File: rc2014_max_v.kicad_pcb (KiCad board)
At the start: 2 copper layers, 101.6 x 50.8 mm, 12 parts, among them IC1 SN74ALVC164245DGG, IC2 5M570ZT100I5N, IC3 SN74ALVC164245DGG, J1 Z80 Bus, J2 Pro Bus, J4 M3 Mounting Hole, U1 MIC5356-SGYMME, U2 SN74AVC8T245PW

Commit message: reorganized pins
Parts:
- removed IC1, IC3: SN74ALVC164245DGG, Package_SO:TSSOP-48_6.1x12.5mm_P0.5mm
- removed IC2: 5M570ZT100I5N, QFP50P1600X1600X120-100N:QFP50P1600X1600X120-100N
- added C10: 100nF, Capacitor_SMD:C_0805_2012Metric_Pad1.15x1.40mm_HandSolder, F.Cu at (101.9, 91.8)
- added C11: 100nF, Capacitor_SMD:C_0805_2012Metric_Pad1.15x1.40mm_HandSolder, F.Cu at (96.0, 103.5)
- added C12: 100nF, Capacitor_SMD:C_0805_2012Metric_Pad1.15x1.40mm_HandSolder, F.Cu at (101.6, 95.9)
- added C13: 100nF, Capacitor_SMD:C_0805_2012Metric_Pad1.15x1.40mm_HandSolder, F.Cu at (106.7, 91.8)
- added C14: 100nF, Capacitor_SMD:C_0805_2012Metric_Pad1.15x1.40mm_HandSolder, F.Cu at (101.5, 103.5)
- added C15: 100nF, Capacitor_SMD:C_0805_2012Metric_Pad1.15x1.40mm_HandSolder, F.Cu at (106.4, 95.9)
- added C16: 100nF, Capacitor_SMD:C_0805_2012Metric_Pad1.15x1.40mm_HandSolder, F.Cu at (106.4, 98.9)
- added C5: 100nF, Capacitor_SMD:C_0805_2012Metric_Pad1.15x1.40mm_HandSolder, F.Cu at (92.4, 91.8)
- added C6: 100nF, Capacitor_SMD:C_0805_2012Metric_Pad1.15x1.40mm_HandSolder, F.Cu at (101.6, 115.4)
- added C7: 100nF, Capacitor_SMD:C_0805_2012Metric_Pad1.15x1.40mm_HandSolder, F.Cu at (97.2, 91.8)
- added C8: 100nF, Capacitor_SMD:C_0805_2012Metric_Pad1.15x1.40mm_HandSolder, F.Cu at (96.1, 115.4)
- added C9: 100nF, Capacitor_SMD:C_0805_2012Metric_Pad1.15x1.40mm_HandSolder, F.Cu at (96.9, 95.9)
- added U3: SN74ALVC164245DGG, Package_SO:TSSOP-48_6.1x12.5mm_P0.5mm, F.Cu at (97.7, 109.4)
- added U4: 5M570ZT100I5N, Package_QFP:TQFP-100_14x14mm_P0.5mm, F.Cu at (130.0, 88.9)
- added U5: SN74ALVC164245DGG, Package_SO:TSSOP-48_6.1x12.5mm_P0.5mm, F.Cu at (154.9, 109.0)
- C1, C2, C3, C4: footprint Capacitor_THT:C_Disc_D3.8mm_W2.6mm_P2.50mm -> Capacitor_SMD:C_0805_2012Metric_Pad1.15x1.40mm_HandSolder; moved to B.Cu
- U1: moved to B.Cu
- U2: value SN74AVC8T245PW -> SN74ALVC164245DGG; footprint Package_SO:TSSOP-24_4.4x7.8mm_P0.65mm -> Package_SO:TSSOP-48_6.1x12.5mm_P0.5mm
- moved C2 35.3 mm to (125.8, 117.9)
- moved C4 35.3 mm to (131.4, 117.9)
- moved U1 35.3 mm to (127.8, 113.6)
- moved C3 35.3 mm to (133.0, 113.4)
- moved U2 6.77 mm to (132.5, 109.0)
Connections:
- J1 pad 20: (no net) -> ~RESET
- J1 pad 22: (no net) -> ~INT
- J2 pad 10: (no net) -> ~NMI
- J2 pad 4: (no net) -> ~RESET2
- J2 pad 7: (no net) -> ~HALT
- J2 pad 8: (no net) -> ~BUSRQ
- J2 pad 9: (no net) -> ~WAIT
- U2 pad 1: (no net) -> DIR
- U2 pad 10: (no net) -> GND
- U2 pad 11: Net-(U2-Pad11) -> ~PAGE
- U2 pad 12: Net-(U2-Pad11) -> ~BUSACK
- U2 pad 13: Net-(U2-Pad11) -> ~RESET
- U2 pad 14: (no net) -> ~INT
- U2 pad 15: (no net) -> GND
- U2 pad 16: (no net) -> ~RESET2
- U2 pad 17: (no net) -> ~HALT
- U2 pad 18: (no net) -> 5V
- U2 pad 19: (no net) -> ~BUSRQ
- U2 pad 2: (no net) -> ~M1
- U2 pad 20: (no net) -> ~WAIT
- U2 pad 21: (no net) -> GND
- U2 pad 22: (no net) -> ~NMI
- U2 pad 24: (no net) -> ~DIR
- U2 pad 3: (no net) -> CLK
- U2 pad 4: (no net) -> GND
- U2 pad 5: (no net) -> ~MREQ
- U2 pad 6: (no net) -> ~WR
- U2 pad 7: (no net) -> 5V
- U2 pad 8: (no net) -> ~RD
- U2 pad 9: (no net) -> ~IORQ

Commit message: numerous changes
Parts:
- removed C13, C15: 100nF, Capacitor_SMD:C_0805_2012Metric_Pad1.15x1.40mm_HandSolder
- added C17: 100nF, Capacitor_SMD:C_0603_1608Metric_Pad1.05x0.95mm_HandSolder, F.Cu at (102.1, 83.3)
- added C18: 100nF, Capacitor_SMD:C_0603_1608Metric_Pad1.05x0.95mm_HandSolder, B.Cu at (95.2, 115.6)
- added C19: 100nF, Capacitor_SMD:C_0603_1608Metric_Pad1.05x0.95mm_HandSolder, B.Cu at (100.8, 115.6)
- added C20: 100nF, Capacitor_SMD:C_0603_1608Metric_Pad1.05x0.95mm_HandSolder, F.Cu at (128.0, 114.3)
- added C21: 100nF, Capacitor_SMD:C_0603_1608Metric_Pad1.05x0.95mm_HandSolder, F.Cu at (132.6, 114.3)
- added C22: 100nF, Capacitor_SMD:C_0603_1608Metric_Pad1.05x0.95mm_HandSolder, F.Cu at (157.2, 114.8)
- added C23: 100nF, Capacitor_SMD:C_0603_1608Metric_Pad1.05x0.95mm_HandSolder, F.Cu at (163.1, 114.8)
- added C24: 100nF, Capacitor_SMD:C_0603_1608Metric_Pad1.05x0.95mm_HandSolder, F.Cu at (126.2, 79.2)
- added C25: 100nF, Capacitor_SMD:C_0603_1608Metric_Pad1.05x0.95mm_HandSolder, F.Cu at (133.9, 79.2)
- added C26: 100nF, Capacitor_SMD:C_0603_1608Metric_Pad1.05x0.95mm_HandSolder, F.Cu at (133.7, 98.6)
- added C27: 100nF, Capacitor_SMD:C_0603_1608Metric_Pad1.05x0.95mm_HandSolder, F.Cu at (139.7, 90.7)
- added C28: 100nF, Capacitor_SMD:C_0603_1608Metric_Pad1.05x0.95mm_HandSolder, F.Cu at (119.4, 86.9)
- added C29: 100nF, Capacitor_SMD:C_0603_1608Metric_Pad1.05x0.95mm_HandSolder, F.Cu at (126.5, 98.6)
- added J3: Conn_01x06, Connector_PinHeader_2.54mm:PinHeader_1x06_P2.54mm_Horizontal, F.Cu at (173.0, 81.3)
- added J5: AVR-JTAG-10, Connector_IDC:IDC-Header_2x05_P2.54mm_Vertical, F.Cu at (159.5, 80.8)
- added J6: Conn_01x06, Connector_PinHeader_2.54mm:PinHeader_1x06_P2.54mm_Horizontal, F.Cu at (173.0, 98.0)
- added R1: 22R5, Resistor_SMD:R_0603_1608Metric_Pad1.05x0.95mm_HandSolder, F.Cu at (115.3, 85.9)
- added R2: 1K, Resistor_SMD:R_0603_1608Metric_Pad1.05x0.95mm_HandSolder, F.Cu at (110.0, 95.5)
- added R3: 1K, Resistor_SMD:R_0603_1608Metric_Pad1.05x0.95mm_HandSolder, F.Cu at (105.4, 95.5)
- added R4: 1K, Resistor_SMD:R_0603_1608Metric_Pad1.05x0.95mm_HandSolder, F.Cu at (107.7, 95.5)
- added SW1: SW_DIP_x03, Button_Switch_SMD:SW_DIP_SPSTx03_Slide_6.7x9.18mm_W8.61mm_P2.54mm_LowProfile, F.Cu at (96.8, 93.7)
- added U6: SN74ALVC164245DGG, Package_SO:TSSOP-48_6.1x12.5mm_P0.5mm, F.Cu at (160.0, 108.7)
- added X1: CB3LV-3I-50M0000, Oscillator:Oscillator_SMD_SeikoEpson_SG8002CA-4Pin_7.0x5.0mm_HandSoldering, F.Cu at (107.7, 83.3)
- C1, C10, C11, C12, C14, C16, C2, C3, C4, C7, C8, C9: footprint Capacitor_SMD:C_0805_2012Metric_Pad1.15x1.40mm_HandSolder -> Capacitor_SMD:C_0603_1608Metric_Pad1.05x0.95mm_HandSolder
- C5, C6: footprint Capacitor_SMD:C_0805_2012Metric_Pad1.15x1.40mm_HandSolder -> Capacitor_SMD:C_0603_1608Metric_Pad1.05x0.95mm_HandSolder; moved to B.Cu
- U2: value SN74ALVC164245DGG -> LTC6930IMS8 7.3728MHz; footprint Package_SO:TSSOP-48_6.1x12.5mm_P0.5mm -> Package_SO:MSOP-8_3x3mm_P0.65mm
- moved C10 62.1 mm to (163.1, 102.6)
- moved C9 60.2 mm to (156.7, 102.6)
- moved U5 57.7 mm to (97.3, 108.7)
- moved C12 39.2 mm to (139.7, 86.9), turned to 90 degrees
- moved C8 38.5 mm to (132.6, 103.1)
- moved U3 32.1 mm to (129.8, 108.7)
- moved C7 31.9 mm to (127.0, 103.1)
- moved C16 30.8 mm to (130.0, 79.2), turned to 180 degrees
- moved U2 30.4 mm to (107.7, 91.4), turned to 0 degrees
- moved C14 28.9 mm to (130.0, 98.6), turned to 180 degrees
- moved C11 26.6 mm to (119.4, 90.7), turned to 270 degrees
- moved C6 13.3 mm to (100.8, 102.1)
- moved C2 12.6 mm to (113.5, 114.8), turned to 180 degrees
- moved C5 10.7 mm to (95.2, 102.1)
- moved U1 9.49 mm to (118.6, 115.8)
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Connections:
- C10 pad 1: 5V -> +3V3
- C11 pad 1: +3V3 -> +1V8
- C12 pad 1: +3V3 -> +1V8
- C14 pad 1: +3V3 -> +1V8
- C16 pad 1: +3V3 -> +1V8
- C2 pad 2: Net-(C2-Pad2) -> GND
- C3 pad 2: Net-(C2-Pad2) -> GND
- C4 pad 2: Net-(C2-Pad2) -> GND
- C5 pad 1: 5V -> +3V3
- C6 pad 1: 5V -> +3V3
- C7 pad 1: 5V -> +3V3
- C8 pad 1: 5V -> +3V3
- C9 pad 1: 5V -> +3V3
- U1 pad 2: Net-(C2-Pad2) -> GND
- U1 pad 3: (no net) -> 5V
- U1 pad 9: Net-(C2-Pad2) -> GND
- U2 pad 1: DIR -> +3V3
- U2 pad 2: ~M1 -> GND
- U2 pad 3: CLK -> Net-(R4-Pad1)
- U2 pad 4: GND -> Net-(R3-Pad1)
- U2 pad 5: ~MREQ -> Net-(R2-Pad1)
- U2 pad 6: ~WR -> GND
- U2 pad 7: 5V -> (no net)
- U2 pad 8: ~RD -> +3V3
- U3 pad 11: A9 -> ~PAGE
- U3 pad 12: A8 -> ~BUSACK
- U3 pad 13: A7 -> ~RESET
- U3 pad 14: A6 -> ~INT
- U3 pad 16: A5 -> ~RESET2
- U3 pad 17: A4 -> ~HALT
- U3 pad 19: A3 -> ~BUSRQ
- U3 pad 2: A15 -> ~M1
- U3 pad 20: A2 -> ~WAIT
- U3 pad 22: A1 -> ~NMI
- U3 pad 23: A0 -> (no net)
- U3 pad 24: DIR -> ~DIR
- U3 pad 3: A14 -> CLK
- U3 pad 5: A13 -> ~MREQ
- U3 pad 6: A12 -> ~WR
- U3 pad 8: A11 -> ~RD
- U3 pad 9: A10 -> ~IORQ
- U4 pad 13: +3V3 -> +1V8
- U4 pad 31: +1V8 -> +3V3
- U4 pad 39: +3V3 -> +1V8
- U4 pad 45: +1V8 -> +3V3
- U4 pad 59: +1V8 -> +3V3
- U4 pad 63: +3V3 -> +1V8
- U4 pad 80: +1V8 -> +3V3
- U4 pad 88: +3V3 -> +1V8
- U4 pad 9: +1V8 -> +3V3
- U4 pad 94: +1V8 -> +3V3
- U5 pad 11: ~PAGE -> A9
- U5 pad 12: ~BUSACK -> A8
- U5 pad 13: D0 -> A7
- U5 pad 14: D1 -> A6
- U5 pad 16: D2 -> A5
- U5 pad 17: D3 -> A4
- U5 pad 19: D4 -> A3
- U5 pad 2: ~M1 -> A15
- U5 pad 20: D5 -> A2
- U5 pad 22: D6 -> A1
- U5 pad 23: D7 -> A0
- U5 pad 24: ~DIR -> DIR
- U5 pad 3: CLK -> A14
- U5 pad 5: ~MREQ -> A13
- U5 pad 6: ~WR -> A12
- U5 pad 8: ~RD -> A11
- U5 pad 9: ~IORQ -> A10
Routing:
- net +3V3: track 0.00 -> 56.8 mm, vias 0 -> 3
- net GND: track 6.54 -> 62.1 mm, vias 0 -> 4
- net 5V: track 6.16 -> 40.2 mm, vias 0 -> 2
- net Net-(R2-Pad1): track 0.00 -> 26.3 mm
- net A15: track 0.00 -> 20.5 mm
- net A0: track 0.72 -> 20.8 mm
- net Net-(R3-Pad1): track 0.00 -> 18.4 mm
- net A14: track 0.00 -> 18.3 mm
- net A1: track 0.00 -> 18.1 mm
- net A13: track 0.00 -> 17.7 mm
- net A2: track 0.00 -> 17.4 mm
- net A12: track 0.00 -> 16.8 mm
- net A3: track 0.36 -> 17.0 mm
- net A11: track 0.00 -> 16.3 mm
- net A4: track 0.73 -> 16.8 mm
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
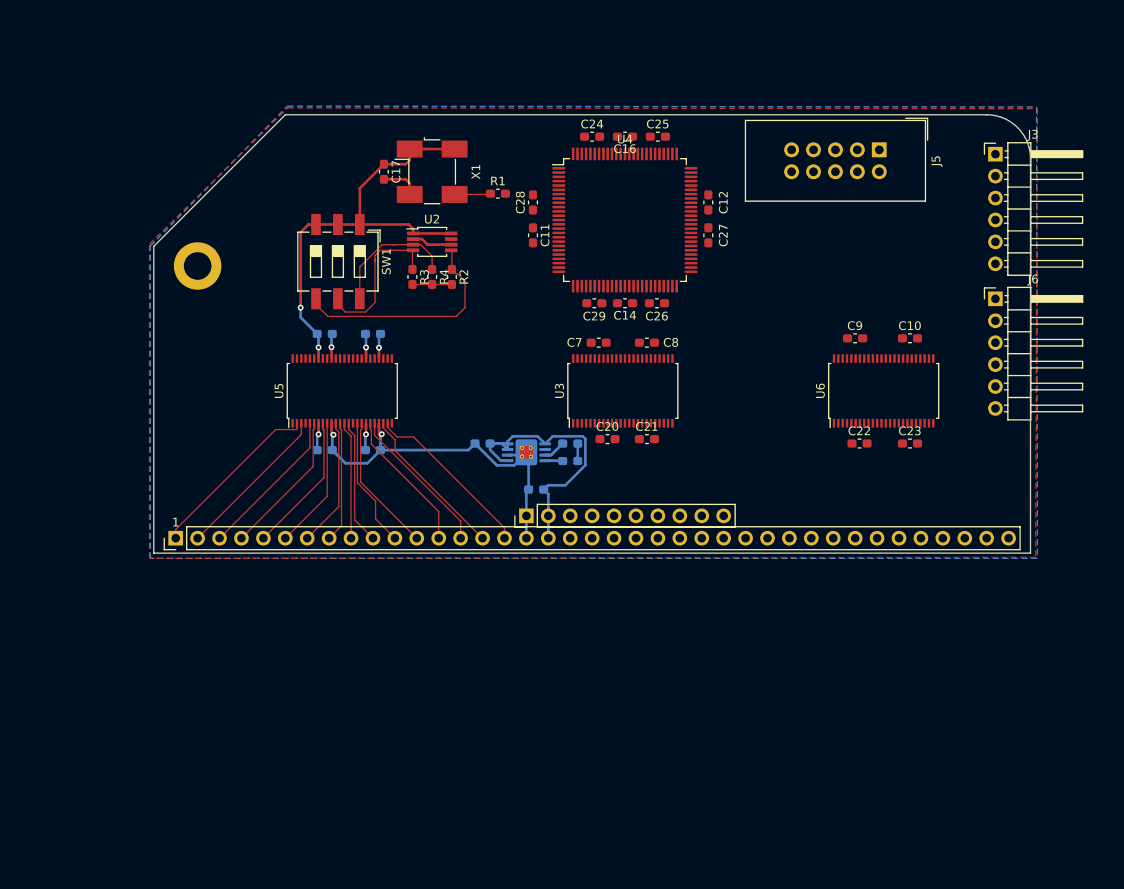
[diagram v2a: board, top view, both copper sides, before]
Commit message: added FT JTAG
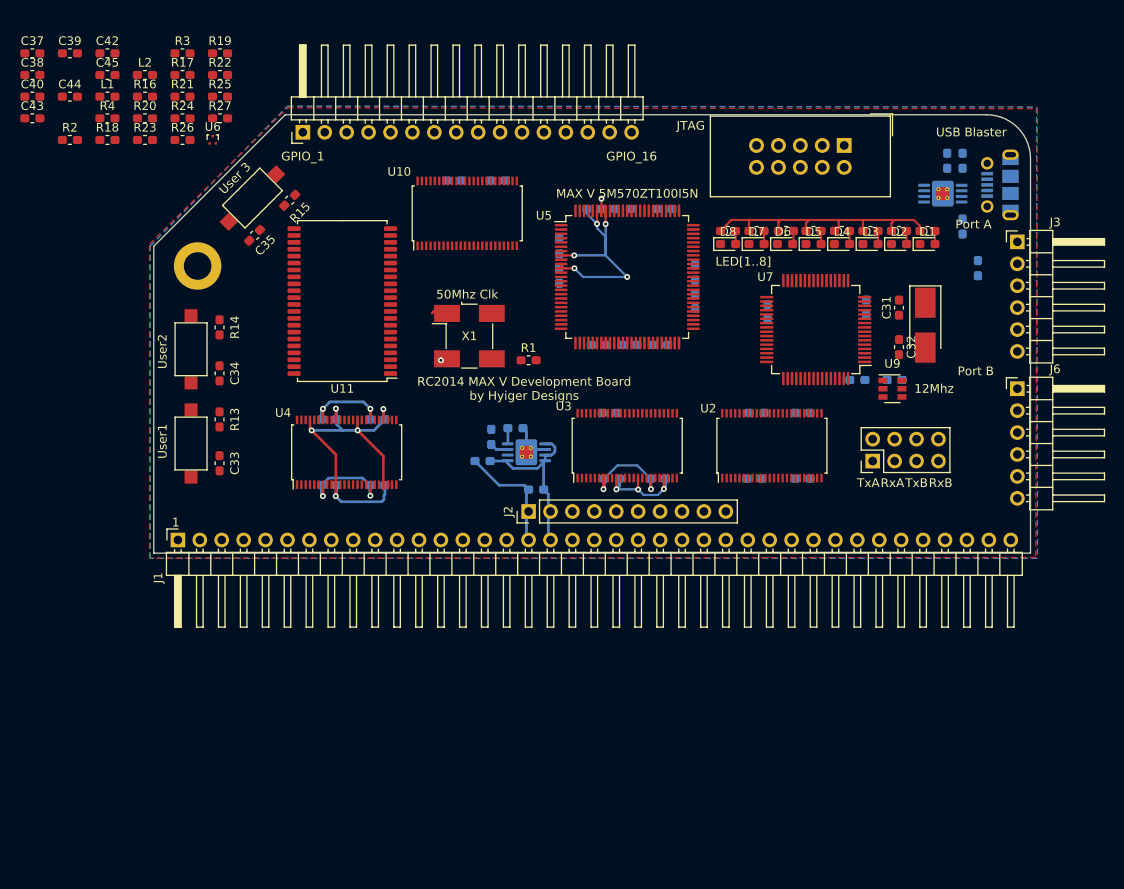
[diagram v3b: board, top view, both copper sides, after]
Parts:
- removed SW1: SW_DIP_x03, Button_Switch_SMD:SW_DIP_SPSTx03_Slide_6.7x9.18mm_W8.61mm_P2.54mm_LowProfile
- added C13: 100nF, Capacitor_SMD:C_0603_1608Metric_Pad1.05x0.95mm_HandSolder, B.Cu at (145.3, 111.3)
- added C15: 100nF, Capacitor_SMD:C_0603_1608Metric_Pad1.05x0.95mm_HandSolder, B.Cu at (128.3, 111.3)
- added C30: 100nF, Capacitor_SMD:C_0603_1608Metric_Pad1.05x0.95mm_HandSolder, B.Cu at (167.4, 82.0)
- added C31: 18pF, Capacitor_SMD:C_0603_1608Metric_Pad1.05x0.95mm_HandSolder, F.Cu at (161.8, 99.1)
- added C32: 18pF, Capacitor_SMD:C_0603_1608Metric_Pad1.05x0.95mm_HandSolder, F.Cu at (161.8, 103.6)
- added C33: 100nF, Capacitor_SMD:C_0603_1608Metric_Pad1.05x0.95mm_HandSolder, F.Cu at (83.1, 117.1)
- added C34: 100nF, Capacitor_SMD:C_0603_1608Metric_Pad1.05x0.95mm_HandSolder, F.Cu at (83.1, 106.7)
- added C35: 100nF, Capacitor_SMD:C_0603_1608Metric_Pad1.05x0.95mm_HandSolder, F.Cu at (87.1, 90.7)
- added C36: 100nF, Capacitor_SMD:C_0603_1608Metric_Pad1.05x0.95mm_HandSolder, B.Cu at (110.2, 84.3)
- added C37: 4.7uF, Capacitor_SMD:C_0603_1608Metric_Pad1.05x0.95mm_HandSolder, F.Cu at (61.4, 69.6)
- added C38: 100nF, Capacitor_SMD:C_0603_1608Metric_Pad1.05x0.95mm_HandSolder, F.Cu at (61.4, 72.1)
- added C39: 4.7uF, Capacitor_SMD:C_0603_1608Metric_Pad1.05x0.95mm_HandSolder, F.Cu at (65.7, 69.6)
- added C40: 100nF, Capacitor_SMD:C_0603_1608Metric_Pad1.05x0.95mm_HandSolder, F.Cu at (61.4, 74.6)
- added C41: 100nF, Capacitor_SMD:C_0603_1608Metric_Pad1.05x0.95mm_HandSolder, B.Cu at (170.9, 94.5)
- added C42: 100nF, Capacitor_SMD:C_0603_1608Metric_Pad1.05x0.95mm_HandSolder, F.Cu at (70.1, 69.6)
- added C43: 100nF, Capacitor_SMD:C_0603_1608Metric_Pad1.05x0.95mm_HandSolder, F.Cu at (61.4, 77.1)
- added C44: 100nF, Capacitor_SMD:C_0603_1608Metric_Pad1.05x0.95mm_HandSolder, F.Cu at (65.7, 74.6)
- added C45: 100nF, Capacitor_SMD:C_0603_1608Metric_Pad1.05x0.95mm_HandSolder, F.Cu at (70.1, 72.1)
- added C46: 100nF, Capacitor_SMD:C_0603_1608Metric_Pad1.05x0.95mm_HandSolder, B.Cu at (158.0, 99.1)
- added C47: 100nF, Capacitor_SMD:C_0603_1608Metric_Pad1.05x0.95mm_HandSolder, B.Cu at (146.6, 99.6)
- added C48: 100nF, Capacitor_SMD:C_0603_1608Metric_Pad1.05x0.95mm_HandSolder, B.Cu at (157.0, 107.4)
- added D1: Blue, LED_SMD:LED_0603_1608Metric_Pad1.05x0.95mm_HandSolder, F.Cu at (165.1, 91.7)
- added D2: Blue, LED_SMD:LED_0603_1608Metric_Pad1.05x0.95mm_HandSolder, F.Cu at (161.8, 91.7)
- added D3: Blue, LED_SMD:LED_0603_1608Metric_Pad1.05x0.95mm_HandSolder, F.Cu at (158.5, 91.7)
- added D4: Blue, LED_SMD:LED_0603_1608Metric_Pad1.05x0.95mm_HandSolder, F.Cu at (155.2, 91.7)
- added D5: Blue, LED_SMD:LED_0603_1608Metric_Pad1.05x0.95mm_HandSolder, F.Cu at (151.9, 91.7)
- added D6: Blue, LED_SMD:LED_0603_1608Metric_Pad1.05x0.95mm_HandSolder, F.Cu at (148.6, 91.7)
- added D7: Blue, LED_SMD:LED_0603_1608Metric_Pad1.05x0.95mm_HandSolder, F.Cu at (145.3, 91.7)
- added D8: Blue, LED_SMD:LED_0603_1608Metric_Pad1.05x0.95mm_HandSolder, F.Cu at (142.0, 91.7)
- added J7: USB_B_Micro, Connector_USB:USB_Micro-B_Molex-105017-0001, B.Cu at (173.5, 84.8)
- added J8: Pro Bus, Connector_PinHeader_2.54mm:PinHeader_1x16_P2.54mm_Horizontal, F.Cu at (92.7, 78.7)
- added J9: Conn_02x04_Counter_Clockwise, Connector_PinHeader_2.54mm:PinHeader_2x04_P2.54mm_Vertical, F.Cu at (158.8, 116.8)
- added L1: 600ohm, Inductor_SMD:L_0603_1608Metric_Pad1.05x0.95mm_HandSolder, F.Cu at (70.1, 74.6)
- added L2: 600ohm, Inductor_SMD:L_0603_1608Metric_Pad1.05x0.95mm_HandSolder, F.Cu at (74.4, 72.1)
- added R10: 220, Resistor_SMD:R_0603_1608Metric_Pad1.05x0.95mm_HandSolder, F.Cu at (148.7, 90.2)
- added R11: 220, Resistor_SMD:R_0603_1608Metric_Pad1.05x0.95mm_HandSolder, F.Cu at (145.3, 90.2)
- added R12: 220, Resistor_SMD:R_0603_1608Metric_Pad1.05x0.95mm_HandSolder, F.Cu at (142.0, 90.2)
- added R13: 10K, Resistor_SMD:R_0603_1608Metric_Pad1.05x0.95mm_HandSolder, F.Cu at (83.1, 112.0)
- added R14: 10K, Resistor_SMD:R_0603_1608Metric_Pad1.05x0.95mm_HandSolder, F.Cu at (83.1, 101.3)
- added R15: 10K, Resistor_SMD:R_0603_1608Metric_Pad1.05x0.95mm_HandSolder, F.Cu at (91.2, 86.6)
- added R16: 10K, Resistor_SMD:R_0603_1608Metric_Pad1.05x0.95mm_HandSolder, F.Cu at (74.4, 74.6)
- added R17: 10K, Resistor_SMD:R_0603_1608Metric_Pad1.05x0.95mm_HandSolder, F.Cu at (78.8, 72.1)
- added R18: 10K, Resistor_SMD:R_0603_1608Metric_Pad1.05x0.95mm_HandSolder, F.Cu at (70.1, 79.6)
- added R19: 2K2, Resistor_SMD:R_0603_1608Metric_Pad1.05x0.95mm_HandSolder, F.Cu at (83.1, 69.6)
- added R20: 10K, Resistor_SMD:R_0603_1608Metric_Pad1.05x0.95mm_HandSolder, F.Cu at (74.4, 77.1)
- added R21: 10K, Resistor_SMD:R_0603_1608Metric_Pad1.05x0.95mm_HandSolder, F.Cu at (78.8, 74.6)
- added R22: 10K, Resistor_SMD:R_0603_1608Metric_Pad1.05x0.95mm_HandSolder, F.Cu at (83.1, 72.1)
- added R23: 10K, Resistor_SMD:R_0603_1608Metric_Pad1.05x0.95mm_HandSolder, F.Cu at (74.4, 79.6)
- added R24: 22R, Resistor_SMD:R_0603_1608Metric_Pad1.05x0.95mm_HandSolder, F.Cu at (78.8, 77.1)
- added R25: 22R, Resistor_SMD:R_0603_1608Metric_Pad1.05x0.95mm_HandSolder, F.Cu at (83.1, 74.6)
- added R26: 22R, Resistor_SMD:R_0603_1608Metric_Pad1.05x0.95mm_HandSolder, F.Cu at (78.8, 79.6)
- added R27: 22R, Resistor_SMD:R_0603_1608Metric_Pad1.05x0.95mm_HandSolder, F.Cu at (83.1, 77.1)
- added R5: 220, Resistor_SMD:R_0603_1608Metric_Pad1.05x0.95mm_HandSolder, F.Cu at (165.1, 90.2)
- added R6: 220, Resistor_SMD:R_0603_1608Metric_Pad1.05x0.95mm_HandSolder, F.Cu at (161.8, 90.2)
- added R7: 220, Resistor_SMD:R_0603_1608Metric_Pad1.05x0.95mm_HandSolder, F.Cu at (158.5, 90.2)
- added R8: 220, Resistor_SMD:R_0603_1608Metric_Pad1.05x0.95mm_HandSolder, F.Cu at (155.2, 90.2)
- added R9: 220, Resistor_SMD:R_0603_1608Metric_Pad1.05x0.95mm_HandSolder, F.Cu at (151.9, 90.2)
- added SW2: SW_Push, Button_Switch_SMD:SW_SPST_CK_RS282G05A3, F.Cu at (79.8, 114.8)
- added SW3: SW_Push, Button_Switch_SMD:SW_SPST_CK_RS282G05A3, F.Cu at (79.8, 103.9)
- added SW4: SW_Push, Button_Switch_SMD:SW_SPST_CK_RS282G05A3, F.Cu at (86.9, 86.4)
- added U10: SN74ALVC164245DGG, Package_SO:TSSOP-48_6.1x12.5mm_P0.5mm, F.Cu at (111.8, 88.1)
- added U11: IS61LV5128AL-10TLI, Package_SO:TSOP-II-44_10.16x18.41mm_P0.8mm, F.Cu at (97.3, 98.3)
- added U7: FT2232H, Package_QFP:LQFP-64_10x10mm_P0.5mm, F.Cu at (152.1, 101.6)
- added U8: MIC5356-SGYMME, Package_SO:MSOP-8-1EP_3x3mm_P0.65mm_EP2.5x3mm_Mask1.73x2.36mm_ThermalVias, B.Cu at (166.9, 85.9)
- added U9: 93LCxxBxxOT, Package_TO_SOT_SMD:SOT-23-6, F.Cu at (161.0, 108.5)
- added Y1: CTS-445 12Mhz, Crystal:Crystal_SMD_5032-2Pin_5.0x3.2mm_HandSoldering, F.Cu at (164.8, 101.1)
- C10, C11, C12, C14, C16, C17, C20, C21, C22, C23, C24, C25, C26, C27, C28, C7, C8, C9: moved to B.Cu
- C29: value 100nF -> 2.2uF; moved to B.Cu
- J1: value Z80 Bus -> Conn_01x39; footprint Connector_PinHeader_2.54mm:PinHeader_1x39_P2.54mm_Vertical -> Connector_PinHeader_2.54mm:PinHeader_1x39_P2.54mm_Horizontal
- J2: value Pro Bus -> Conn_01x10
- R2: value 1K -> 12K
- R4: value 1K -> 1M
- U2: value LTC6930IMS8 7.3728MHz -> SN74ALVC164245DGG; footprint Package_SO:MSOP-8_3x3mm_P0.65mm -> Package_SO:TSSOP-48_6.1x12.5mm_P0.5mm
- U4: value 5M570ZT100I5N -> SN74ALVC164245DGG; footprint Package_QFP:TQFP-100_14x14mm_P0.5mm -> Package_SO:TSSOP-48_6.1x12.5mm_P0.5mm
- U5: value SN74ALVC164245DGG -> 5M570ZT100I5N; footprint Package_SO:TSSOP-48_6.1x12.5mm_P0.5mm -> Package_QFP:TQFP-100_14x14mm_P0.5mm
- U6: value SN74ALVC164245DGG -> TPD2EUSB30; footprint Package_SO:TSSOP-48_6.1x12.5mm_P0.5mm -> Package_TO_SOT_SMD:Texas_DRT-3
- moved U6 83.0 mm to (82.3, 79.6), turned to 0 degrees
- moved C28 50.0 mm to (169.2, 82.0)
- moved C18 48.3 mm to (134.6, 87.6)
- moved R2 47.0 mm to (65.7, 79.6), turned to 0 degrees
- moved U2 45.9 mm to (147.1, 115.1), turned to 90 degrees
- moved C12 45.9 mm to (101.3, 112.0), turned to 0 degrees
- moved C29 43.6 mm to (169.2, 89.7), turned to 90 degrees
- moved C23 43.0 mm to (129.8, 87.6), turned to 180 degrees
- moved C16 42.1 mm to (161.3, 107.4)
- moved U4 42.0 mm to (97.8, 115.8), turned to 90 degrees
- moved R4 41.9 mm to (70.1, 77.1), turned to 0 degrees
- moved C22 41.6 mm to (122.4, 91.9), turned to 90 degrees
- moved C19 41.1 mm to (138.2, 98.3), turned to 90 degrees
- moved R3 37.2 mm to (78.8, 69.6), turned to 0 degrees
- moved U5 35.6 mm to (130.3, 95.5), turned to 0 degrees
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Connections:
- C10 pad 1: +3V3 -> 5V
- C11 pad 1: +1V8 -> +3V3
- C12 pad 1: +1V8 -> +3V3
- C14 pad 1: +1V8 -> +3V3
- C16 pad 1: +1V8 -> +3V3
- C18 pad 1: 5V -> +3V3
- C19 pad 1: 5V -> +3V3
- C20 pad 1: 5V -> +3V3
- C21 pad 1: 5V -> +3V3
- C22 pad 1: 5V -> +3V3
- C23 pad 1: 5V -> +1V8
- C24 pad 1: +3V3 -> +1V8
- C25 pad 1: +3V3 -> +1V8
- C26 pad 1: +3V3 -> +1V8
- C28 pad 1: +3V3 -> +1V8
- C29 pad 1: +3V3 -> Net-(C29-Pad1)
- C5 pad 1: +3V3 -> 5V
- C6 pad 1: +3V3 -> 5V
- C7 pad 1: +3V3 -> 5V
- C8 pad 1: +3V3 -> 5V
- C9 pad 1: +3V3 -> 5V
- J5 pad 1: (no net) -> JTAG_TCK
- J5 pad 10: Net-(J5-Pad10) -> GND
- J5 pad 2: Net-(J5-Pad10) -> GND
- J5 pad 3: (no net) -> JTAG_TDO
- J5 pad 5: (no net) -> JTAG_TMS
- J5 pad 9: (no net) -> JTAG_TDI
- R2 pad 1: Net-(R2-Pad1) -> GND
- R3 pad 1: Net-(R3-Pad1) -> +3V3
- R3 pad 2: Net-(R2-Pad2) -> Net-(R3-Pad2)
- R4 pad 1: Net-(R4-Pad1) -> Net-(C41-Pad1)
- R4 pad 2: Net-(R2-Pad2) -> GND
- U2 pad 1: +3V3 -> DIR
- U2 pad 2: GND -> ~M1
- U2 pad 3: Net-(R4-Pad1) -> CLK
- U2 pad 4: Net-(R3-Pad1) -> GND
- U2 pad 5: Net-(R2-Pad1) -> ~MREQ
- U2 pad 6: GND -> ~WR
- U2 pad 7: (no net) -> 5V
- U2 pad 8: +3V3 -> ~RD
- U3 pad 1: DIR -> ~DIR
- U3 pad 11: ~PAGE -> ~NMI
- U3 pad 12: ~BUSACK -> (no net)
- U3 pad 13: ~RESET -> (no net)
- U3 pad 14: ~INT -> (no net)
- U3 pad 16: ~RESET2 -> (no net)
- U3 pad 17: ~HALT -> (no net)
- U3 pad 19: ~BUSRQ -> (no net)
- U3 pad 2: ~M1 -> ~RESET
- U3 pad 20: ~WAIT -> (no net)
- U3 pad 22: ~NMI -> (no net)
- U3 pad 24: ~DIR -> (no net)
- U3 pad 3: CLK -> ~INT
- U3 pad 5: ~MREQ -> ~RESET2
- U3 pad 6: ~WR -> ~HALT
- U3 pad 8: ~RD -> ~BUSRQ
- U3 pad 9: ~IORQ -> ~WAIT
- U4 pad 1: (no net) -> DIR
- U4 pad 11: GND -> A9
- U4 pad 12: (no net) -> A8
- U4 pad 13: +1V8 -> A7
- U4 pad 14: (no net) -> A6
- U4 pad 15: (no net) -> GND
- U4 pad 16: (no net) -> A5
- U4 pad 17: (no net) -> A4
- U4 pad 18: (no net) -> 5V
- U4 pad 19: (no net) -> A3
- U4 pad 2: (no net) -> A15
- U4 pad 20: (no net) -> A2
- U4 pad 21: (no net) -> GND
- U4 pad 22: (no net) -> A1
- U4 pad 23: (no net) -> A0
- U4 pad 24: (no net) -> DIR
- U4 pad 25: (no net) -> OE_A
- U4 pad 26: (no net) -> A0_F
- U4 pad 27: (no net) -> A1_F
- U4 pad 28: (no net) -> GND
- U4 pad 29: (no net) -> A2_F
- U4 pad 3: (no net) -> A14
- U4 pad 30: (no net) -> A3_F
- U4 pad 32: GND -> A4_F
- U4 pad 33: (no net) -> A5_F
- U4 pad 34: (no net) -> GND
- U4 pad 35: (no net) -> A6_F
- U4 pad 36: (no net) -> A7_F
- U4 pad 37: GND -> A8_F
- U4 pad 38: (no net) -> A9_F
- U4 pad 39: +1V8 -> GND
- U4 pad 4: (no net) -> GND
- U4 pad 40: (no net) -> A10_F
- U4 pad 41: (no net) -> A11_F
- U4 pad 42: (no net) -> +3V3
- U4 pad 43: (no net) -> A12_F
- U4 pad 44: (no net) -> A13_F
- U4 pad 45: +3V3 -> GND
- U4 pad 46: GND -> A14_F
- U4 pad 47: (no net) -> A15_F
- U4 pad 48: (no net) -> OE_A
- U4 pad 5: (no net) -> A13
- U4 pad 6: (no net) -> A12
- U4 pad 7: (no net) -> 5V
- U4 pad 8: GND -> A11
- U4 pad 9: +3V3 -> A10
- U5 pad 1: DIR -> (no net)
- U5 pad 11: A9 -> GND
- U5 pad 12: A8 -> (no net)
- U5 pad 13: A7 -> +1V8
- U5 pad 14: A6 -> (no net)
- U5 pad 15: GND -> (no net)
- U5 pad 16: A5 -> (no net)
- U5 pad 17: A4 -> (no net)
- U5 pad 18: 5V -> (no net)
- U5 pad 19: A3 -> (no net)
- U5 pad 2: A15 -> (no net)
- U5 pad 20: A2 -> (no net)
- U5 pad 21: GND -> (no net)
- U5 pad 22: A1 -> (no net)
- U5 pad 23: A0 -> (no net)
- U5 pad 24: DIR -> (no net)
- U5 pad 28: GND -> (no net)
- U5 pad 3: A14 -> (no net)
- U5 pad 32: (no net) -> GND
- U5 pad 34: GND -> (no net)
- U5 pad 37: (no net) -> GND
- U5 pad 39: GND -> +1V8
- U5 pad 4: GND -> (no net)
- U5 pad 42: +3V3 -> (no net)
- U5 pad 45: GND -> +3V3
- U5 pad 46: (no net) -> GND
- U5 pad 5: A13 -> (no net)
- U5 pad 6: A12 -> (no net)
- U5 pad 7: 5V -> (no net)
- U5 pad 8: A11 -> GND
- U5 pad 9: A10 -> +3V3
- U6 pad 1: DIR -> Net-(J7-Pad3)
- U6 pad 2: ~M1 -> Net-(J7-Pad2)
- U6 pad 3: CLK -> GND
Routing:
- net GND: track 62.1 -> 107.7 mm, vias 4 -> 14
- net Net-(R2-Pad1): track 26.3 -> 0.00 mm
- net A15: track 20.5 -> 0.00 mm
- net A0: track 20.8 -> 1.20 mm
- net Net-(R3-Pad1): track 18.4 -> 0.00 mm
- net A14: track 18.3 -> 0.00 mm
- net A1: track 18.1 -> 0.43 mm
- net A13: track 17.7 -> 0.12 mm
- net A2: track 17.4 -> 0.00 mm
- net A12: track 16.8 -> 0.00 mm
- net A3: track 17.0 -> 0.36 mm
- net A11: track 16.3 -> 0.00 mm
- net A4: track 16.8 -> 0.73 mm
- net Net-(R4-Pad1): track 15.6 -> 0.00 mm
- net A10: track 15.3 -> 0.00 mm
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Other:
- board text added: "12Mhz"
- board text added: "50Mhz Clk"
- board text added: "GPIO_1"
- board text added: "GPIO_16"
- board text added: "JTAG"
- board text added: "LED[1..8]"
- board text added: "MAX V 5M570ZT100I5N"
- board text added: "Port A"
- board text added: "Port B"
- board text added: "RC2014 MAX V Development Board by Hyiger Designs"
- board text added: "RxA"
- board text added: "RxB"
- board text added: "TxA"
- board text added: "TxB"
- board text added: "USB Blaster"
- board text added: "User 3"
- board text added: "User1"
- board text added: "User2"
